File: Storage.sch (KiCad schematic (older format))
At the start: 19 parts, among them J8 Micro_SD_Card_Det, U17 FTDITypeUART, U18 ABRACON-ASDMB, U19 S25FL256SAGNFI001, U8 xc7z020clg400

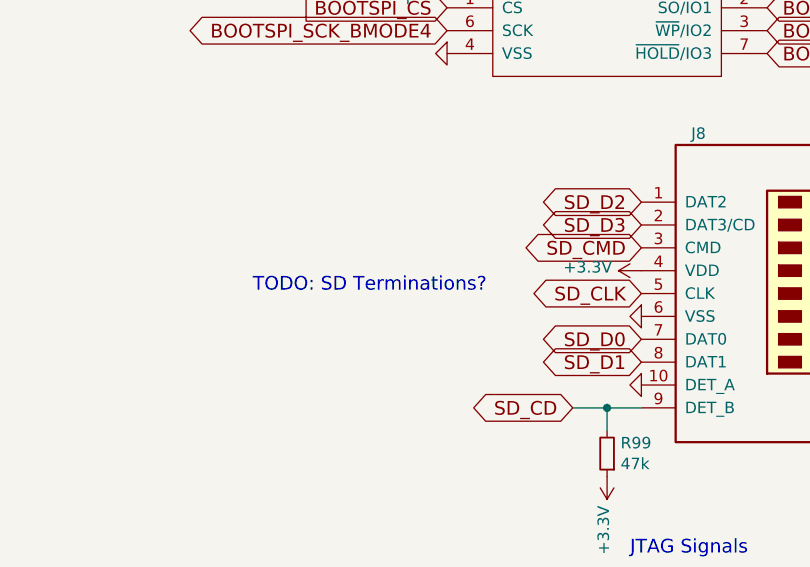
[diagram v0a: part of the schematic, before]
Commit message: replacing rescue components foreal
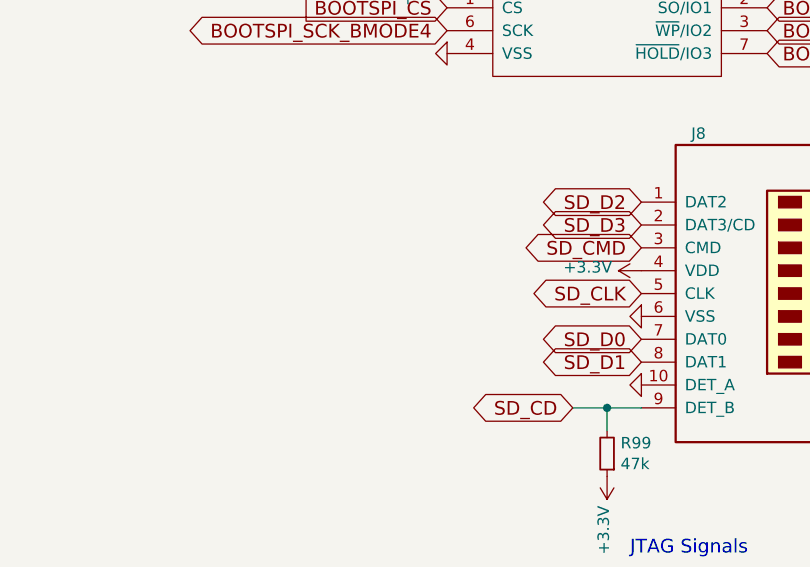
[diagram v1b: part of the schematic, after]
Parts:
- U8: footprint Package_BGA:BGA-400_21.0x21.0mm_Layout20x20_P1.0mm -> DFTcustom:BGA400_0.8p_17mmx17mm
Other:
- note removed: "TODO: SD Terminations?\n"
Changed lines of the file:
@@
 F 0 "U8" H 5850 1800 60  0000 L CNN
 F 1 "xc7z020clg400" H 5600 1700 60  0000 L CNN
-F 2 "Package_BGA:BGA-400_21.0x21.0mm_Layout20x20_P1.0mm" H 5300 1550 60  0001 C CNN
+F 2 "DFTcustom:BGA400_0.8p_17mmx17mm" H 5300 1550 60  0001 C CNN
 F 3 "" H 5300 1550 60  0001 C CNN
 	5    5300 1550
@@
 Text Notes 4500 3000 0    60   ~ 0
 I2C3v3 or GPIO \ncan go here\n
-Text Notes 2350 5650 0    60   ~ 0
-TODO: SD Terminations?\n
 Text GLabel 5300 3250 0    60   Input ~ 0
 ZYNQ_POR

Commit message: still works, miraculously
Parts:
- C120, C121, C122: footprint Capacitors_SMD:C_0603 -> Capacitor_SMD:C_0603_1608Metric; symbol DFTBoard-rescue:C_Small- -> Device:C_Small
- C123: footprint Capacitors_SMD:C_1210 -> Capacitor_SMD:C_1210_3225Metric; symbol DFTBoard-rescue:C_Small- -> Device:C_Small
- R91, R92, R93, R94, R95, R96, R97: symbol DFTBoard-rescue:R_Small -> Device:R_Small
- R98: symbol DFTBoard-rescue:R- -> Device:R
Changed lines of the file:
@@
 SD_CMD
 $Comp
-L DFTBoard-rescue:GND-RESCUE-DFTBoard- #PWR?
+L power:GND #PWR?
 U 1 1 5CA20F30
 P 4050 5750
@@
 SD_D1
 $Comp
-L DFTBoard-rescue:GND-RESCUE-DFTBoard- #PWR?
+L power:GND #PWR?
 U 1 1 5CA20F39
 P 5800 6300
@@
 RF_IRQ
 $Comp
-L DFTBoard-rescue:GND-RESCUE-DFTBoard- #PWR?
+L power:GND #PWR?
 U 1 1 5CA20F42
 P 4050 6050
@@
 SD_CD
 $Comp
-L DFTBoard-rescue:+3.3V #PWR?
+L power:+3V3 #PWR?
 U 1 1 5CA20F4B
 P 4050 5550
@@
 RF2_IRQ
 $Comp
-L DFTBoard-rescue:C_Small- C?
+L Device:C_Small C?
 U 1 1 5CA20F60
 P 5050 3450
@@
 F 0 "C123" H 5060 3520 50  0000 L CNN
 F 1 "100uF" H 5060 3370 50  0000 L CNN
-F 2 "Capacitors_SMD:C_1210" H 5050 3450 50  0001 C CNN
+F 2 "Capacitor_SMD:C_1210_3225Metric" H 5050 3450 50  0001 C CNN
 F 3 "" H 5050 3450 50  0001 C CNN
 F 4 "TAIYO YUDEN" H 1550 -1600 50  0001 C CNN "MFR"
@@
 $EndComp
 $Comp
-L DFTBoard-rescue:C_Small- C?
+L Device:C_Small C?
 U 1 1 5CA20F6C
 P 4550 3450
@@
 F 0 "C121" H 4560 3520 50  0000 L CNN
 F 1 ".47uF" H 4560 3370 50  0000 L CNN
-F 2 "Capacitors_SMD:C_0603" H 4550 3450 50  0001 C CNN
+F 2 "Capacitor_SMD:C_0603_1608Metric" H 4550 3450 50  0001 C CNN
 F 3 "" H 4550 3450 50  0001 C CNN
 F 4 "Murata" H 2600 -2300 50  0001 C CNN "MFR"
@@
 $EndComp
 $Comp
-L DFTBoard-rescue:C_Small- C?
+L Device:C_Small C?
 U 1 1 5CA20F78
 P 4800 3450
@@
 F 0 "C122" H 4810 3520 50  0000 L CNN
 F 1 "4.7uF" H 4810 3370 50  0000 L CNN
-F 2 "Capacitors_SMD:C_0603" H 4800 3450 50  0001 C CNN
+F 2 "Capacitor_SMD:C_0603_1608Metric" H 4800 3450 50  0001 C CNN
 F 3 "" H 4800 3450 50  0001 C CNN
 F 4 "Murata" H 2250 -2300 50  0001 C CNN "MFR"
@@
 	4800 3600 4800 3650
 $Comp
-L DFTBoard-rescue:GND-RESCUE-DFTBoard- #PWR?
+L power:GND #PWR?
 U 1 1 5CA20F89
 P 4800 3650
@@
 Connection ~ 5050 3350
 $Comp
-L DFTBoard-rescue:+3.3V #PWR?
+L power:+3V3 #PWR?
 U 1 1 5CA20F91
 P 4550 3350
@@
 	3900 6150 3750 6150
 $Comp
-L DFTBoard-rescue:+3.3V #PWR?
+L power:+3V3 #PWR?
 U 1 1 5CA20FAB
 P 3900 6450
@@
 $EndComp
 $Comp
-L DFTBoard-rescue:R_Small R?
+L Device:R_Small R?
 U 1 1 5CA20FB1
 P 1600 2450
@@
 	1850 2450 1700 2450
 $Comp
-L DFTBoard-rescue:R_Small R?
+L Device:R_Small R?
 U 1 1 5CA20FB9
 P 1600 2550
@@
 	1850 2550 1700 2550
 $Comp
-L DFTBoard-rescue:GND-RESCUE-DFTBoard- #PWR?
+L power:GND #PWR?
 U 1 1 5CA20FC1
 P 1300 2450
@@
 $EndComp
 $Comp
-L DFTBoard-rescue:R_Small R?
+L Device:R_Small R?
 U 1 1 5CA20FC7
 P 1600 2350
@@
 	1850 2350 1700 2350
 $Comp
-L DFTBoard-rescue:R_Small R?
+L Device:R_Small R?
 U 1 1 5CA20FCF
 P 1600 1950
@@
 	1850 1950 1700 1950
 $Comp
-L DFTBoard-rescue:R_Small R?
+L Device:R_Small R?
 U 1 1 5CA20FD7
 P 1600 2050
@@
 	1850 2050 1700 2050
 $Comp
-L DFTBoard-rescue:R_Small R?
+L Device:R_Small R?
 U 1 1 5CA20FDF
 P 1600 2150
@@
 $EndComp
 $Comp
-L DFTBoard-rescue:R_Small R?
+L Device:R_Small R?
 U 1 1 5CA20FE6
 P 1600 2250
@@
 	1850 2250 1700 2250
 $Comp
-L DFTBoard-rescue:+3.3V #PWR?
+L power:+3V3 #PWR?
 U 1 1 5CA20FEF
 P 1300 2350
@@
 BOOTSPI_DQ3_BMODE0
 $Comp
-L DFTBoard-rescue:+3.3V #PWR?
+L power:+3V3 #PWR?
 U 1 1 5CA21030
 P 3200 4300
@@
 BOOTSPI_CS
 $Comp
-L DFTBoard-rescue:GND-RESCUE-DFTBoard- #PWR?
+L power:GND #PWR?
 U 1 1 5CA21037
 P 3200 4600
@@
 $EndComp
 $Comp
-L DFTBoard-rescue:GND-RESCUE-DFTBoard- #PWR?
+L power:GND #PWR?
 U 1 1 5CA403E2
 P 2500 1450
@@
 $EndComp
 $Comp
-L DFTBoard-rescue:+3.3V #PWR?
+L power:+3V3 #PWR?
 U 1 1 5CA404EC
 P 2500 950
@@
 $EndComp
 $Comp
-L DFTBoard-rescue:C_Small- C?
+L Device:C_Small C?
 U 1 1 5CA4098B
 P 1900 1150
@@
 F 0 "C120" H 1910 1220 50  0000 L CNN
 F 1 ".01uF" H 1910 1070 50  0000 L CNN
-F 2 "Capacitors_SMD:C_0603" H 1900 1150 50  0001 C CNN
+F 2 "Capacitor_SMD:C_0603_1608Metric" H 1900 1150 50  0001 C CNN
 F 3 "" H 1900 1150 50  0001 C CNN
 F 4 "Murata" H 300 -3400 50  0001 C CNN "MFR"
@@
 $EndComp
 $Comp
-L DFTBoard-rescue:+3.3V #PWR?
+L power:+3V3 #PWR?
 U 1 1 5CA412C3
 P 1900 1050
@@
 $EndComp
 $Comp
-L DFTBoard-rescue:GND-RESCUE-DFTBoard- #PWR?
+L power:GND #PWR?
 U 1 1 5CA41304
 P 1900 1250
@@
 $EndComp
 $Comp
-L DFTBoard-rescue:R- R?
+L Device:R R?
 U 1 1 5CA43B34
 P 2350 1350
@@
 $EndComp
 $Comp
-L DFTBoard-rescue:+3.3V #PWR?
+L power:+3V3 #PWR?
 U 1 1 5CA445CF
 P 2200 1350
@@
 $EndComp
 $Comp
-L DFTBoard-rescue:GND-RESCUE-DFTBoard- #PWR?
+L power:GND #PWR?
 U 1 1 5CA4AD9E
 P 2700 3100
@@
 NoConn ~ 2700 3600
 $Comp
-L DFTBoard-rescue:+3.3V #PWR?
+L power:+3V3 #PWR?
 U 1 1 5CA4C036
 P 2700 3300

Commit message: random updates
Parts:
- removed U8: xc7z020clg400, DFTcustom:BGA400_0.8p_17mmx17mm, symbol DFTBoard-rescue:xc7z020clg400-
- added U20: xc7z020clg484, DFTcustom:BGA-484_19.0x19.0mm_Layout22x22_P0.80mm_dia0.40mm, symbol xilinx7:xc7z020clg484
- C120, C121, C122: footprint Capacitor_SMD:C_0603_1608Metric -> Capacitor_SMD:C_0402_1005Metric
- U17: footprint (none) -> DFTcustom:FTDI_CONN
- U18: footprint manuf:ABRACON-ASDMB -> XTAL_ASDMB-24.000MHZ-LC-T:XTAL_ASDMB-24.000MHZ-LC-T
- U19: footprint (none) -> DFTcustom:WSON-8
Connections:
- net +3V3: now also U20.B3 (VCCO_MIO0_500[2]), U20.C6 (VCCO_MIO0_500[2])
- net BOOTSPI_CS: now also U20.A1 (PS_MIO1_500)
- net BOOTSPI_DQ0_BMODE3: now also U20.A2 (PS_MIO2_500)
- net BOOTSPI_DQ1_BMODE1: now also U20.F6 (PS_MIO3_500)
- net BOOTSPI_DQ2_BMODE2: now also U20.E4 (PS_MIO4_500)
- net BOOTSPI_DQ3_BMODE0: now also U20.A3 (PS_MIO5_500)
- net BOOTSPI_SCK_BMODE4: now also U20.A4 (PS_MIO6_500)
- net RF2_IRQ: now also U20.E6 (PS_MIO15_500)
- net RF_IRQ: now also U20.C4 (PS_MIO9_500)
- net TOUCH_INT#: now also U20.B6 (PS_MIO14_500)
- net TOUCH_RST#: now also U20.G6 (PS_MIO0_500)
- net UART33_RX: now also U20.G7 (PS_MIO10_500)
- net UART33_TX: now also U20.B4 (PS_MIO11_500)
- net VMODE0: now also U20.D5 (PS_MIO7_500)
- net VMODE1: now also U20.E5 (PS_MIO8_500)
- net ZYNQ_POR: now also U20.B5 (PS_POR_B_500)
- net at R100.1: now also U20.F7 (PS_CLK_500)
- new net I2C33_SCLK: U20.C5 (PS_MIO12_500)
- new net I2C33_SDA: U20.A6 (PS_MIO13_500)
- no-connect marks 4 -> 2
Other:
- note removed: "I2C3v3 or GPIO \ncan go here\n"
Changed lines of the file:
@@
 	0    -1   -1   0
-$EndComp
-$Comp
-L DFTBoard-rescue:xc7z020clg400- U?
-U 5 1 5CA20F53
-P 5300 1550
-AR Path="/5852A88E/5CA20F53" Ref="U?"  Part="5"
-AR Path="/5CA1ABAE/5CA20F53" Ref="U8"  Part="5"
-F 0 "U8" H 5850 1800 60  0000 L CNN
-F 1 "xc7z020clg400" H 5600 1700 60  0000 L CNN
-F 2 "DFTcustom:BGA400_0.8p_17mmx17mm" H 5300 1550 60  0001 C CNN
-F 3 "" H 5300 1550 60  0001 C CNN
-	5    5300 1550
-	1    0    0    -1
 $EndComp
 Text GLabel 5300 3150 0    60   BiDi ~ 0
@@
 F 0 "C121" H 4560 3520 50  0000 L CNN
 F 1 ".47uF" H 4560 3370 50  0000 L CNN
-F 2 "Capacitor_SMD:C_0603_1608Metric" H 4550 3450 50  0001 C CNN
+F 2 "Capacitor_SMD:C_0402_1005Metric" H 4550 3450 50  0001 C CNN
 F 3 "" H 4550 3450 50  0001 C CNN
 F 4 "Murata" H 2600 -2300 50  0001 C CNN "MFR"
@@
 F 0 "C122" H 4810 3520 50  0000 L CNN
 F 1 "4.7uF" H 4810 3370 50  0000 L CNN
-F 2 "Capacitor_SMD:C_0603_1608Metric" H 4800 3450 50  0001 C CNN
+F 2 "Capacitor_SMD:C_0402_1005Metric" H 4800 3450 50  0001 C CNN
 F 3 "" H 4800 3450 50  0001 C CNN
 F 4 "Murata" H 2250 -2300 50  0001 C CNN "MFR"
@@
 F 0 "U19" H 3900 4887 60  0000 C CNN
 F 1 "S25FL256SAGNFI001" H 3900 4781 60  0000 C CNN
-F 2 "" H 3500 5400 60  0001 C CNN
+F 2 "DFTcustom:WSON-8" H 3500 5400 60  0001 C CNN
 F 3 "" H 3500 5400 60  0000 C CNN
 	1    3900 4400
@@
 F 0 "U18" H 3000 1575 50  0000 C CNN
 F 1 "ABRACON-ASDMB" H 3000 1484 50  0000 C CNN
-F 2 "manuf:ABRACON-ASDMB" H 3000 750 50  0001 C CNN
+F 2 "XTAL_ASDMB-24.000MHZ-LC-T:XTAL_ASDMB-24.000MHZ-LC-T" H 3000 750 50  0001 C CNN
 F 3 "http://www.abracon.com/Oscillators/ASDMB.pdf" H 3000 650 50  0001 C CNN
 F 4 "Abracon" H 3000 550 50  0001 C CNN "Manuf"
@@
 F 0 "C120" H 1910 1220 50  0000 L CNN
 F 1 ".01uF" H 1910 1070 50  0000 L CNN
-F 2 "Capacitor_SMD:C_0603_1608Metric" H 1900 1150 50  0001 C CNN
+F 2 "Capacitor_SMD:C_0402_1005Metric" H 1900 1150 50  0001 C CNN
 F 3 "" H 1900 1150 50  0001 C CNN
 F 4 "Murata" H 300 -3400 50  0001 C CNN "MFR"
@@
 F 0 "U17" H 2456 3987 60  0000 C CNN
 F 1 "FTDITypeUART" H 2456 3881 60  0000 C CNN
-F 2 "" H 2300 3450 60  0001 C CNN
+F 2 "DFTcustom:FTDI_CONN" H 2300 3450 60  0001 C CNN
 F 3 "" H 2300 3450 60  0001 C CNN
 	1    2400 3400
@@
 Text GLabel 2700 3500 2    60   Output ~ 0
 UART33_TX
-NoConn ~ 5300 2850
-NoConn ~ 5300 2950
-Text Notes 4500 3000 0    60   ~ 0
-I2C3v3 or GPIO \ncan go here\n
 Text GLabel 5300 3250 0    60   Input ~ 0
 ZYNQ_POR
+$Comp
+L xilinx7:xc7z020clg484 U20
+U 6 1 5CD32D26
+P 5300 1550
+F 0 "U20" H 6431 703 60  0000 L CNN
+F 1 "xc7z020clg484" H 6431 597 60  0000 L CNN
+F 2 "DFTcustom:BGA-484_19.0x19.0mm_Layout22x22_P0.80mm_dia0.40mm" H 5300 1550 60  0001 C CNN
+F 3 "" H 5300 1550 60  0001 C CNN
+	6    5300 1550
+	1    0    0    -1
+$EndComp
+Text GLabel 5300 2850 0    60   Output ~ 0
+I2C33_SCLK
+Text GLabel 5300 2950 0    60   BiDi ~ 0
+I2C33_SDA
 $EndSCHEMATC

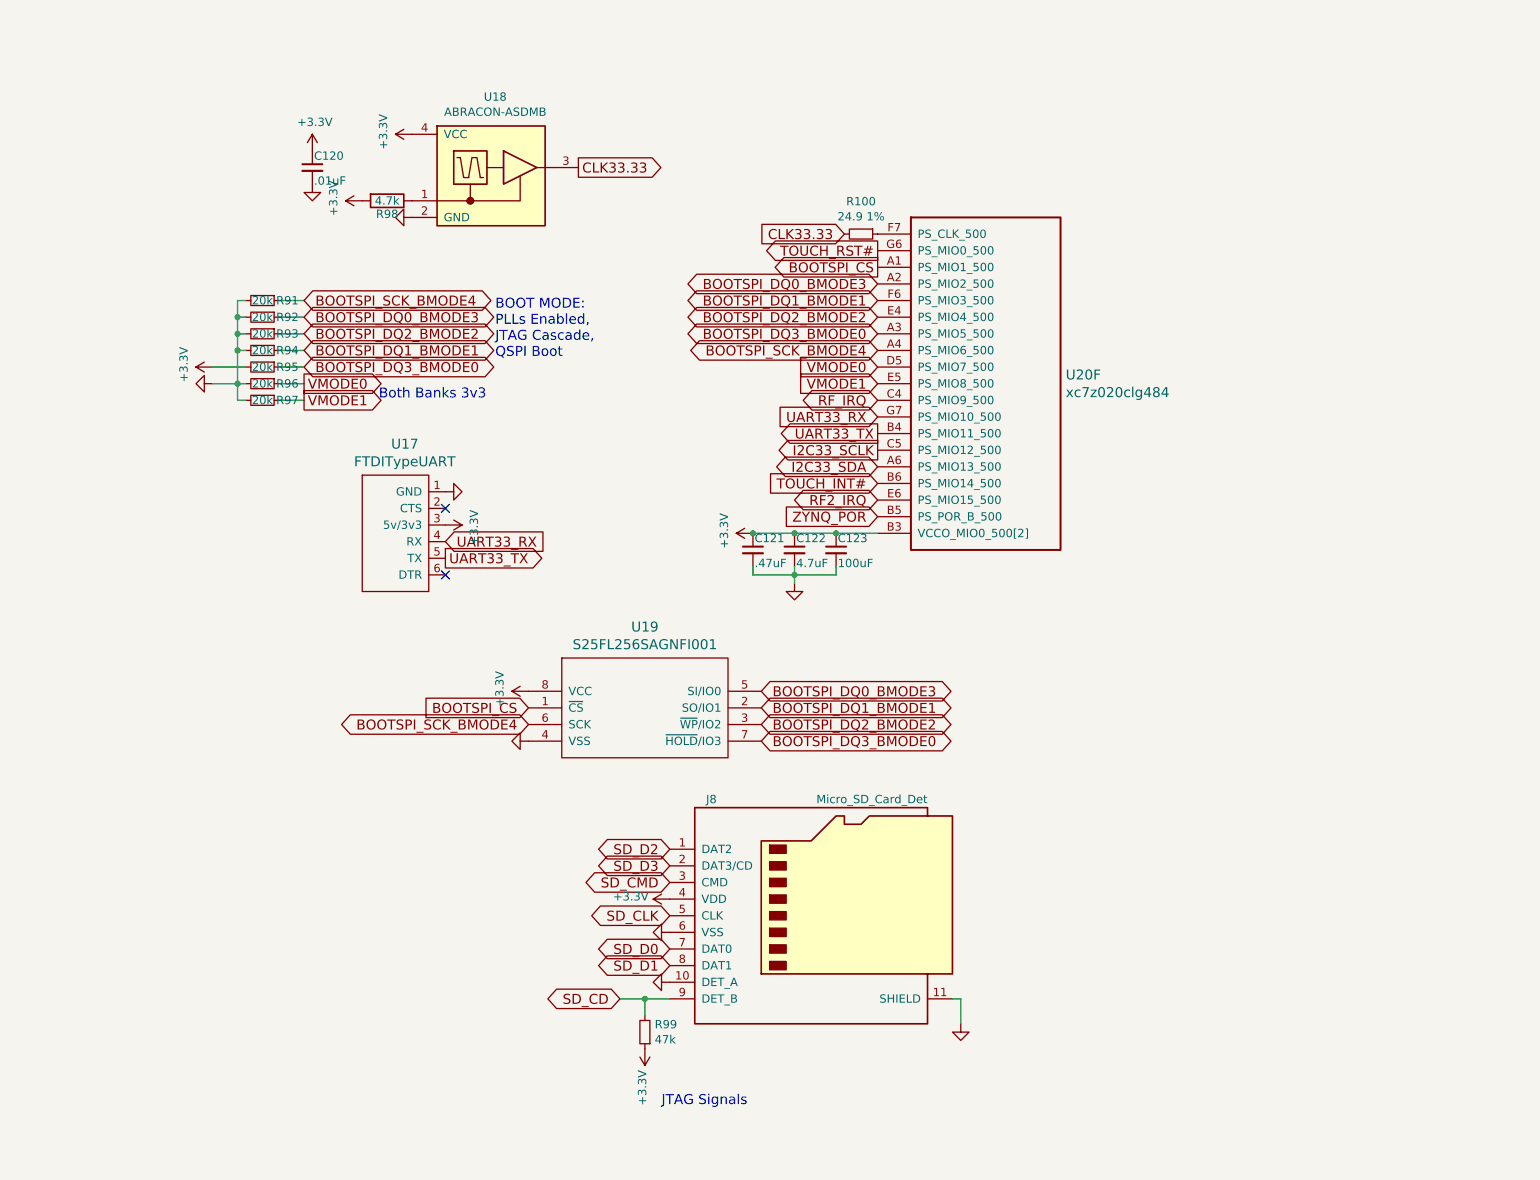
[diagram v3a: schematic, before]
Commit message: everything placed, about to shrink text size globally
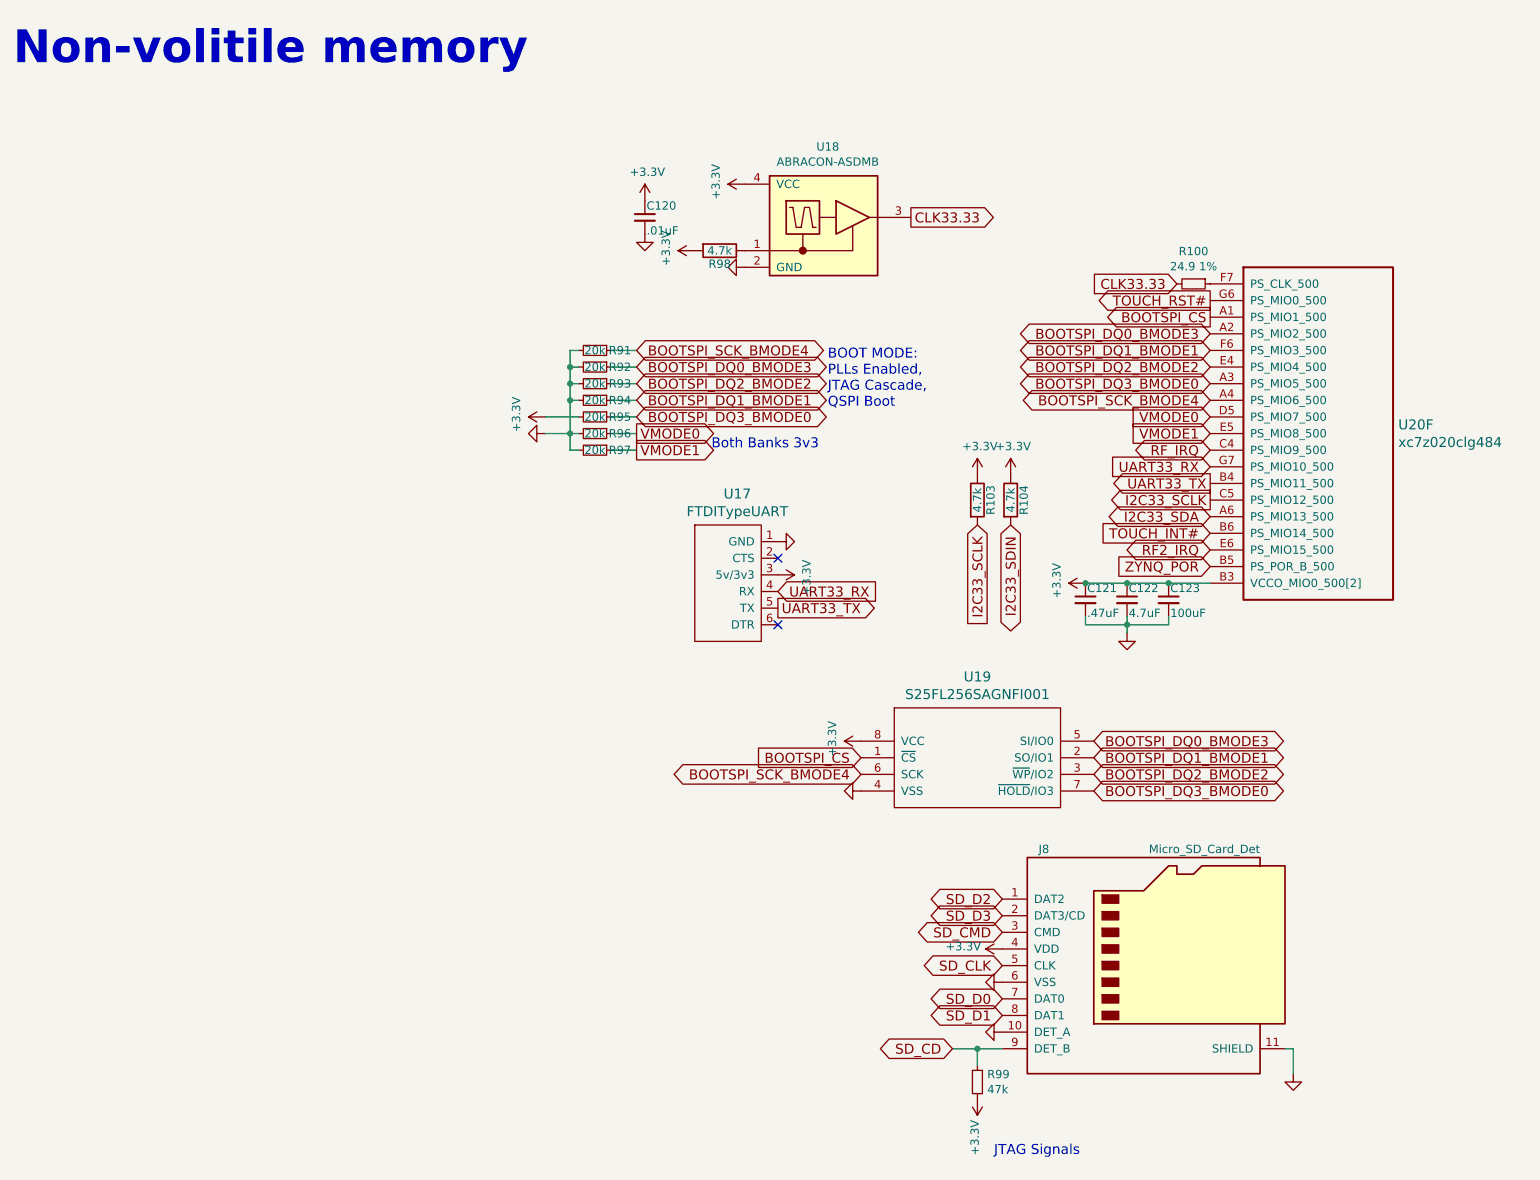
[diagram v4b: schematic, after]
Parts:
- added R103, R104: 4.7k, Resistor_SMD:R_0402_1005Metric, symbol Device:R
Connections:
- net +3V3: now also R103.1, R104.1
- net I2C33_SCLK: now also R103.2
- new net I2C33_SDIN: R104.2
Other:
- note added: "Non-volitile memory"
- moved on the sheet: C120, C121, C122, C123, J8, R100, R91, R92, R93, R94, R95, R96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
